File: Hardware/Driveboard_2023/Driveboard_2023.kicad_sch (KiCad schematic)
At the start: 83 parts, among them J1 6P6C, J2 RJ45_LED_Shielded, SW1 SW_Push, SW2 SW_Push, SW3 SW_Push, SW4 SW_Push, SW5 SW_Push, SW6 SW_Push, SW7 SW_SPDT, U1 Teensy4.1_DEV-16771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

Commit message: Assigned Footprints
Assigned footprints
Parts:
- removed D1, D10, D11, D12, D13, D14, D2, D3, D4, D5, D6, D7, D8, D9: 1N4001, Diode_THT:D_DO-41_SOD81_P10.16mm_Horizontal, symbol Diode:1N4001
- added D1, D10, D11, D12, D2, D3, D4, D5, D6, D7, D8, D9: PMEG3015EH, Diode_SMD:D_SOD-123F, symbol Diode:PMEG3015EH
- Conn1: footprint (none) -> MRDT_Connectors:Anderson_2_Horizontal_Side_by_Side_PV
- Conn2, Conn3, Conn4, Conn5, Conn6, Conn7: footprint (none) -> MRDT_Connectors:MOLEX_SL_03_Horizontal
- R17, R19, R21, R23, R25, R27: value 100 -> 10
- SW7: footprint (none) -> Button_Switch_THT:SW_Slide_1P2T_CK_OS102011MS2Q
- U1: footprint MRDT_Shields:MODULE_DEV-16771 -> MRDT_Shields:Teensy_4_1_Vertical
- U2: footprint (none) -> MRDT_Devices:OKI_Horizontal
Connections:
- net BLRX: no longer U1.21 (A7)
- net BLTX: no longer U1.20 (A6)
- net BRRX: now also U1.21 (A7)
- net BRTX: now also U1.20 (A6)
- net MLRX: no longer U1.16 (A2)
- net MLTX: no longer U1.17 (A3)
- net MRRX: now also U1.16 (A2)
- net MRTX: now also U1.17 (A3)
- net at LED15.2 (A): now also D6.1 (K)
- net at R21.2: now also D6.2 (A)
- net at LED19.2 (A): now also D10.1 (K)
- net at R25.2: now also D10.2 (A)
- net at LED21.2 (A): now also D12.1 (K)
- net at R27.2: now also D12.2 (A)
- net at R24.2: now also D9.2 (A)
- net at LED13.2 (A): now also D4.1 (K)
- net at R19.2: now also D4.2 (A)
- net at LED18.2 (A): now also D9.1 (K)
- net at LED14.2 (A): now also D5.1 (K)
- net at R20.2: now also D5.2 (A)
- net at LED20.2 (A): now also D11.1 (K)
- net at R26.2: now also D11.2 (A)
- net at R22.2: now also D7.2 (A)
- net at LED12.2 (A): now also D3.1 (K)
- net at R18.2: now also D3.2 (A)
- net at R16.2: now also D1.2 (A)
- net at LED17.2 (A): now also D8.1 (K)
- net at R23.2: now also D8.2 (A)
- net at R17.2: now also D2.2 (A)
- net at LED11.2 (A): now also D2.1 (K)
- net at R14.2: now also LED8.2 (A)
- net at LED16.2 (A): now also D7.1 (K)
- net at LED9.2 (A): now also R15.2
- net at LED10.2 (A): now also D1.1 (K)

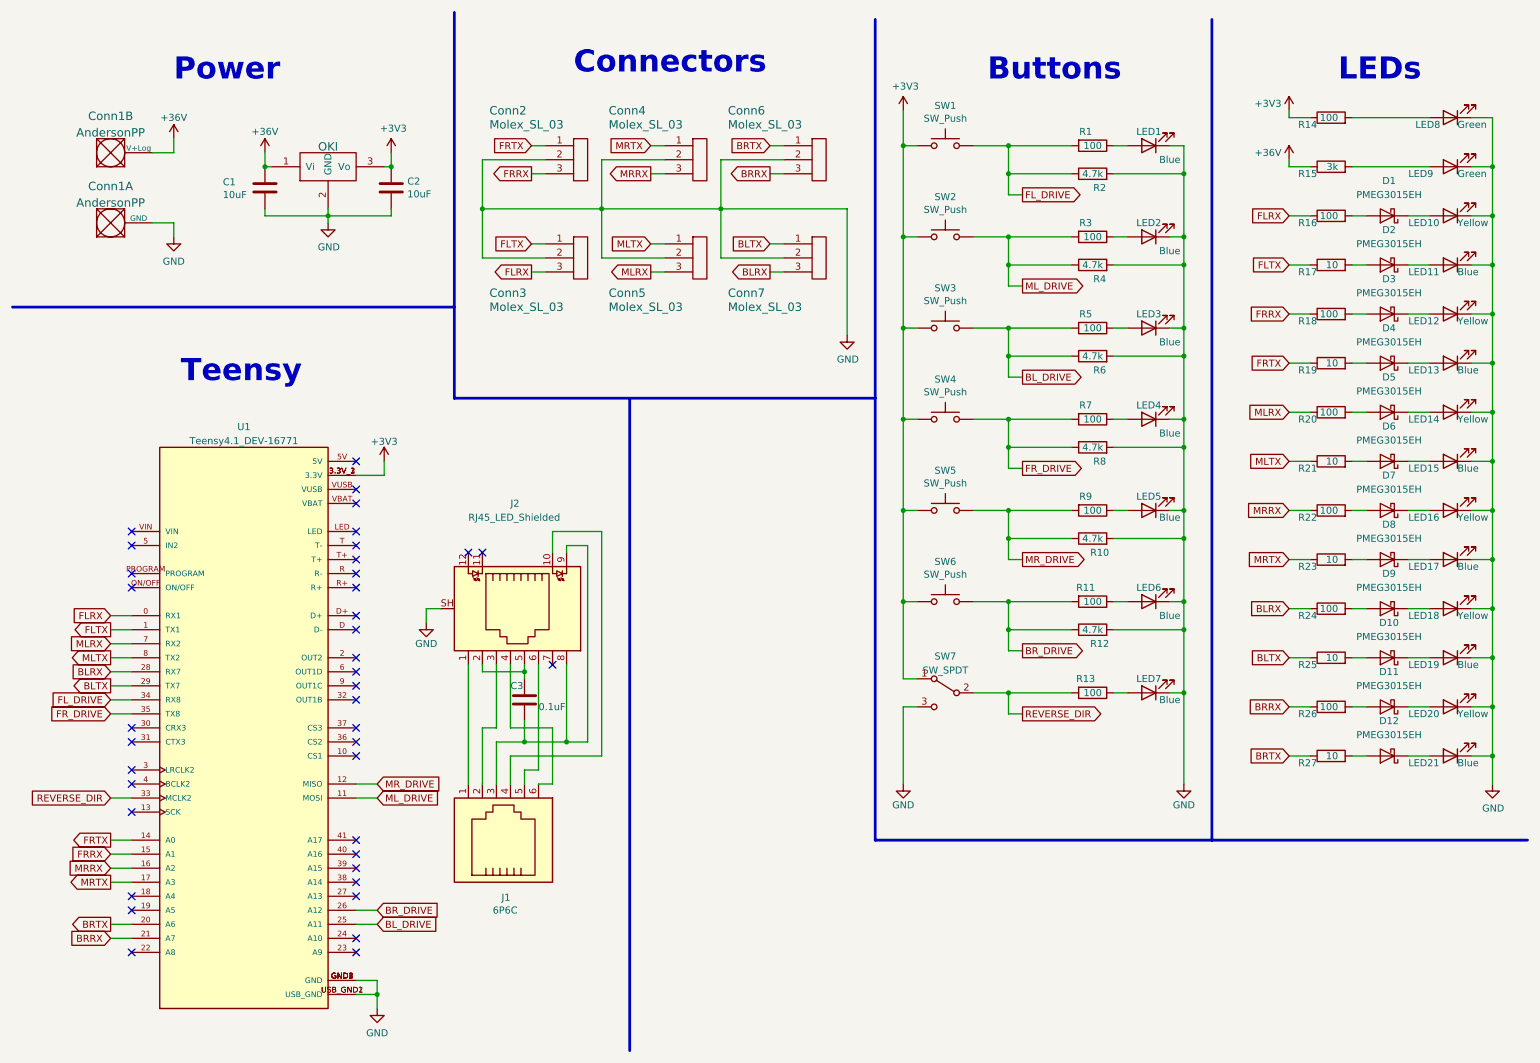
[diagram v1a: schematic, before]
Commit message: PCB Layout
Started and Finished Rev1 of DriveBoard
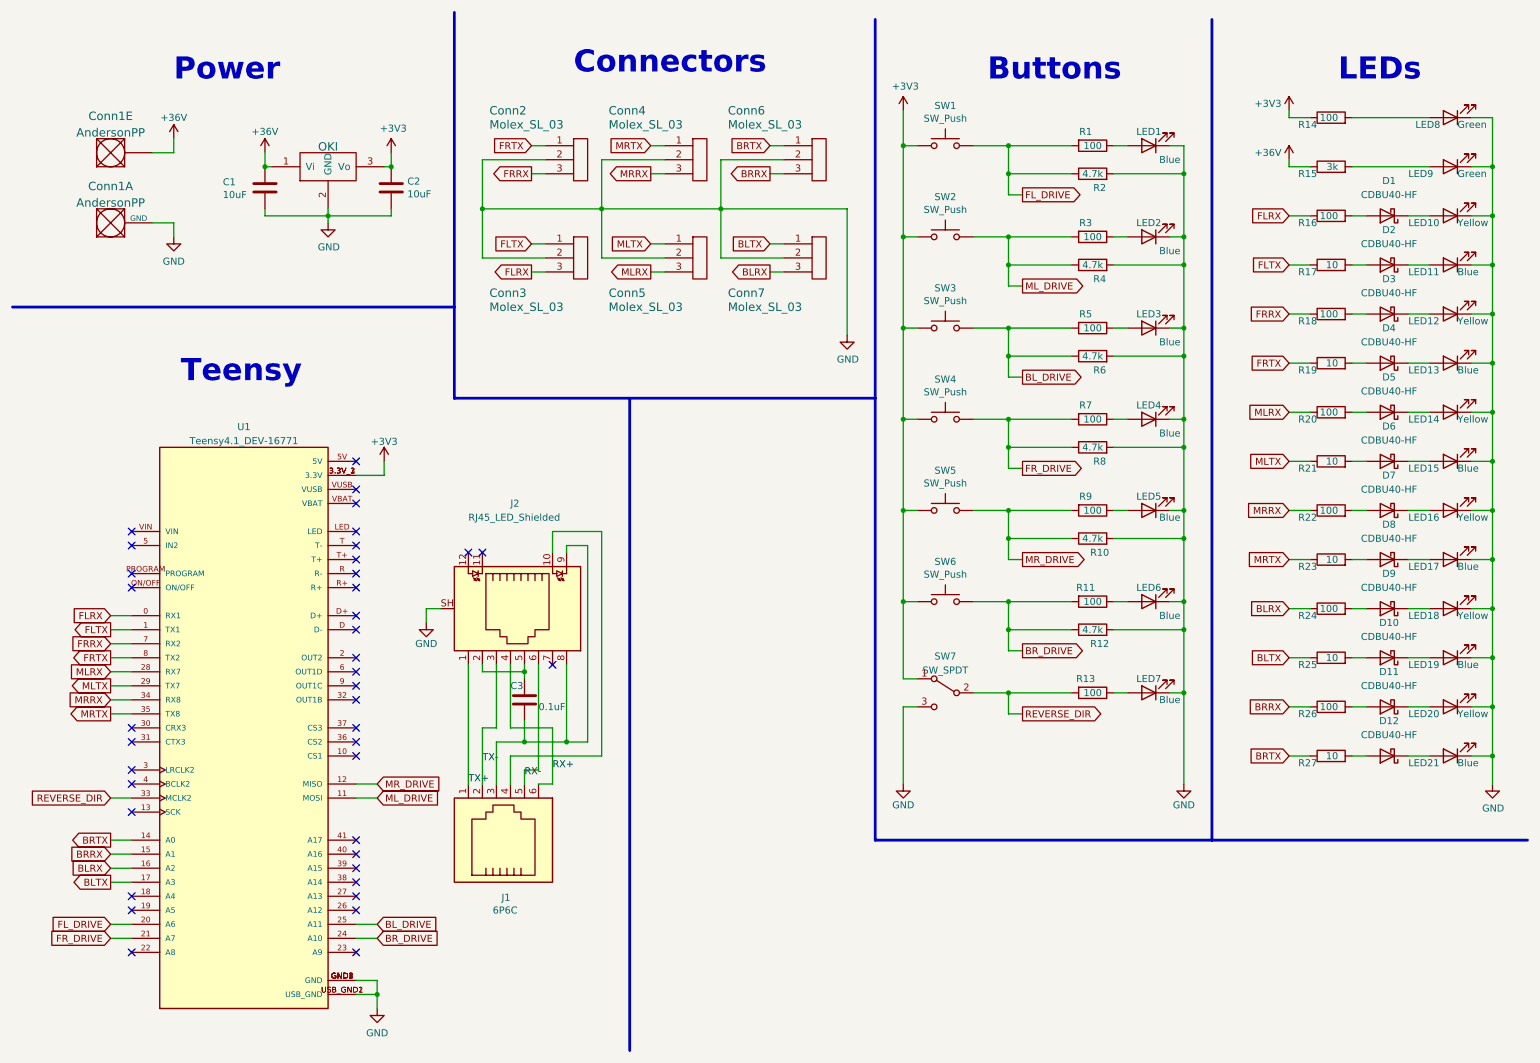
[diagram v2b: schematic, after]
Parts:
- removed D1, D10, D11, D12, D2, D3, D4, D5, D6, D7, D8, D9: PMEG3015EH, Diode_SMD:D_SOD-123F, symbol Diode:PMEG3015EH
- added D1, D10, D11, D12, D2, D3, D4, D5, D6, D7, D8, D9: CDBU40-HF, Diode_SMD:D_0603_1608Metric, symbol Diode:CDBU40-HF
- Conn1: footprint MRDT_Connectors:Anderson_2_Horizontal_Side_by_Side_PV -> MRDT_Connectors:Square_Anderson_2_H_Side_By_Side
- U1: footprint MRDT_Shields:Teensy_4_1_Vertical -> MRDT_Shields:Teensy_4_1
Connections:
- net +36V: now also Conn1.1; no longer Conn1.2 (V+Log)
- net BLRX: now also U1.16 (A2); no longer U1.28 (RX7)
- net BLTX: now also U1.17 (A3); no longer U1.29 (TX7)
- net BRRX: now also U1.15 (A1); no longer U1.21 (A7)
- net BRTX: now also U1.14 (A0); no longer U1.20 (A6)
- net BR_DRIVE: now also U1.24 (A10); no longer U1.26 (A12)
- net FL_DRIVE: now also U1.20 (A6); no longer U1.34 (RX8)
- net FRRX: now also U1.7 (RX2); no longer U1.15 (A1)
- net FRTX: now also U1.8 (TX2); no longer U1.14 (A0)
- net FR_DRIVE: now also U1.21 (A7); no longer U1.35 (TX8)
- net MLRX: now also U1.28 (RX7); no longer U1.7 (RX2)
- net MLTX: now also U1.29 (TX7); no longer U1.8 (TX2)
- net MRRX: now also U1.34 (RX8); no longer U1.16 (A2)
- net MRTX: now also U1.35 (TX8); no longer U1.17 (A3)
- net at R24.2: now also D9.2 (A)
- net at LED20.2 (A): now also D11.1 (K)
- net at R26.2: now also D11.2 (A)
- net at LED21.2 (A): now also D12.1 (K)
- net at LED16.2 (A): now also D7.1 (K)
- net at R22.2: now also D7.2 (A)
- net at LED13.2 (A): now also D4.1 (K)
- net at R19.2: now also D4.2 (A)
- net at LED12.2 (A): now also D3.1 (K)
- net at R18.2: now also D3.2 (A)
- net at LED17.2 (A): now also D8.1 (K)
- net at R23.2: now also D8.2 (A)
- net at LED19.2 (A): now also D10.1 (K)
- net at R25.2: now also D10.2 (A)
- net at LED14.2 (A): now also D5.1 (K)
- net at R20.2: now also D5.2 (A)
- net at LED18.2 (A): now also D9.1 (K)
- net TX+: now reaches J1.1, J2.1
- net TX-: now reaches J1.2, J2.3
- net RX+: now reaches J1.6, J2.4
- net RX-: now reaches J1.5, J2.6
- net at R21.2: now also D6.2 (A)
- net at LED15.2 (A): now also D6.1 (K)
- net at R27.2: now also D12.2 (A)
- net at R16.2: now also D1.2 (A)
- net at R17.2: now also D2.2 (A)
- net at LED11.2 (A): now also D2.1 (K)
- net at LED10.2 (A): now also D1.1 (K)

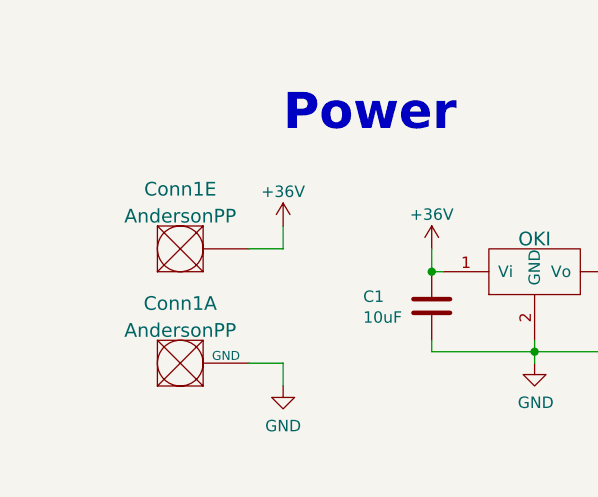
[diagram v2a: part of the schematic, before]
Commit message: Layout Review Board
Finished Changes. Needs to add signatures.
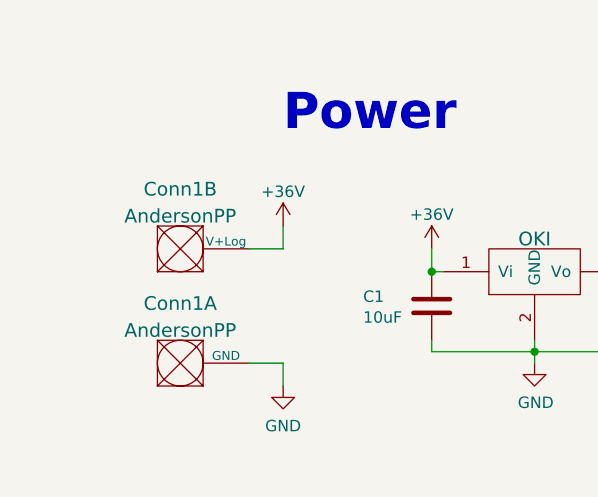
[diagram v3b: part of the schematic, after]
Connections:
- net +36V: now also Conn1.2 (V+Log); no longer Conn1.1
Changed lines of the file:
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@@
     (pin "2")
   )
-  (symbol (lib_id "MRDT_Connectors:AndersonPP") (at 25.4 38.1 0) (unit 5)
+  (symbol (lib_id "MRDT_Connectors:AndersonPP") (at 25.4 38.1 0) (unit 2)
     (in_bom yes) (on_board yes) (fields_autoplaced)
     (property "Reference" "Conn1" (id 0) (at 27.94 28.9359 0)
@@
     )
     (path "/b01ac07b-2202-49d2-b5da-686cdae6ec6c"
-      (reference "Conn1") (unit 5) (value "AndersonPP") (footprint "MRDT_Connectors:Square_Anderson_2_H_Side_By_Side")
+      (reference "Conn1") (unit 2) (value "AndersonPP") (footprint "MRDT_Connectors:Square_Anderson_2_H_Side_By_Side")
     )
     (path "/2efca18a-387a-49fe-a849-7362a7250e39"

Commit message: Layout Review Changes
Fixed the diode's footprints
Labeled many components on PCB
Changed some traces
Added Signature
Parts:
- D1, D10, D11, D12, D2, D3, D4, D5, D6, D7, D8, D9: footprint Diode_SMD:D_0603_1608Metric -> Diode_SMD:D_0603_1608Metric_Pad1.05x0.95mm_HandSolder
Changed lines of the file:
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@@
     (property "Reference" "D9" (id 0) (at 259.3975 111.76 0))
     (property "Value" "CDBU40-HF" (id 1) (at 259.3975 114.3 0))
-    (property "Footprint" "Diode_SMD:D_0603_1608Metric" (id 2) (at 259.08 113.665 0)
+    (property "Footprint" "Diode_SMD:D_0603_1608Metric_Pad1.05x0.95mm_HandSolder" (id 2) (at 259.08 113.665 0)
       (effects (font (size 1.27 1.27)) hide)
     )
@@
     (property "Reference" "D8" (id 0) (at 259.3975 102.87 0))
     (property "Value" "CDBU40-HF" (id 1) (at 259.3975 105.41 0))
-    (property "Footprint" "Diode_SMD:D_0603_1608Metric" (id 2) (at 259.08 104.775 0)
+    (property "Footprint" "Diode_SMD:D_0603_1608Metric_Pad1.05x0.95mm_HandSolder" (id 2) (at 259.08 104.775 0)
       (effects (font (size 1.27 1.27)) hide)
     )
@@
     (property "Reference" "D3" (id 0) (at 259.3975 58.42 0))
     (property "Value" "CDBU40-HF" (id 1) (at 259.3975 60.96 0))
-    (property "Footprint" "Diode_SMD:D_0603_1608Metric" (id 2) (at 259.08 60.325 0)
+    (property "Footprint" "Diode_SMD:D_0603_1608Metric_Pad1.05x0.95mm_HandSolder" (id 2) (at 259.08 60.325 0)
       (effects (font (size 1.27 1.27)) hide)
     )
@@
     (property "Reference" "D10" (id 0) (at 259.3975 120.65 0))
     (property "Value" "CDBU40-HF" (id 1) (at 259.3975 123.19 0))
-    (property "Footprint" "Diode_SMD:D_0603_1608Metric" (id 2) (at 259.08 122.555 0)
+    (property "Footprint" "Diode_SMD:D_0603_1608Metric_Pad1.05x0.95mm_HandSolder" (id 2) (at 259.08 122.555 0)
       (effects (font (size 1.27 1.27)) hide)
     )
@@
     (property "Reference" "D11" (id 0) (at 259.3975 129.54 0))
     (property "Value" "CDBU40-HF" (id 1) (at 259.3975 132.08 0))
-    (property "Footprint" "Diode_SMD:D_0603_1608Metric" (id 2) (at 259.08 131.445 0)
+    (property "Footprint" "Diode_SMD:D_0603_1608Metric_Pad1.05x0.95mm_HandSolder" (id 2) (at 259.08 131.445 0)
       (effects (font (size 1.27 1.27)) hide)
     )
@@
     (property "Reference" "D4" (id 0) (at 259.3975 67.31 0))
     (property "Value" "CDBU40-HF" (id 1) (at 259.3975 69.85 0))
-    (property "Footprint" "Diode_SMD:D_0603_1608Metric" (id 2) (at 259.08 69.215 0)
+    (property "Footprint" "Diode_SMD:D_0603_1608Metric_Pad1.05x0.95mm_HandSolder" (id 2) (at 259.08 69.215 0)
       (effects (font (size 1.27 1.27)) hide)
     )
@@
     (property "Reference" "D6" (id 0) (at 259.3975 85.09 0))
     (property "Value" "CDBU40-HF" (id 1) (at 259.3975 87.63 0))
-    (property "Footprint" "Diode_SMD:D_0603_1608Metric" (id 2) (at 259.08 86.995 0)
+    (property "Footprint" "Diode_SMD:D_0603_1608Metric_Pad1.05x0.95mm_HandSolder" (id 2) (at 259.08 86.995 0)
       (effects (font (size 1.27 1.27)) hide)
     )
@@
     (property "Reference" "D12" (id 0) (at 259.3975 138.43 0))
     (property "Value" "CDBU40-HF" (id 1) (at 259.3975 140.97 0))
-    (property "Footprint" "Diode_SMD:D_0603_1608Metric" (id 2) (at 259.08 140.335 0)
+    (property "Footprint" "Diode_SMD:D_0603_1608Metric_Pad1.05x0.95mm_HandSolder" (id 2) (at 259.08 140.335 0)
       (effects (font (size 1.27 1.27)) hide)
     )
@@
     (property "Reference" "D5" (id 0) (at 259.3975 76.2 0))
     (property "Value" "CDBU40-HF" (id 1) (at 259.3975 78.74 0))
-    (property "Footprint" "Diode_SMD:D_0603_1608Metric" (id 2) (at 259.08 78.105 0)
+    (property "Footprint" "Diode_SMD:D_0603_1608Metric_Pad1.05x0.95mm_HandSolder" (id 2) (at 259.08 78.105 0)
       (effects (font (size 1.27 1.27)) hide)
     )
@@
     (property "Reference" "D7" (id 0) (at 259.3975 93.98 0))
     (property "Value" "CDBU40-HF" (id 1) (at 259.3975 96.52 0))
-    (property "Footprint" "Diode_SMD:D_0603_1608Metric" (id 2) (at 259.08 95.885 0)
+    (property "Footprint" "Diode_SMD:D_0603_1608Metric_Pad1.05x0.95mm_HandSolder" (id 2) (at 259.08 95.885 0)
       (effects (font (size 1.27 1.27)) hide)
     )
@@
     (property "Reference" "D1" (id 0) (at 259.3975 40.64 0))
     (property "Value" "CDBU40-HF" (id 1) (at 259.3975 43.18 0))
-    (property "Footprint" "Diode_SMD:D_0603_1608Metric" (id 2) (at 259.08 42.545 0)
+    (property "Footprint" "Diode_SMD:D_0603_1608Metric_Pad1.05x0.95mm_HandSolder" (id 2) (at 259.08 42.545 0)
       (effects (font (size 1.27 1.27)) hide)
     )
@@
     (property "Reference" "D2" (id 0) (at 259.3975 49.53 0))
     (property "Value" "CDBU40-HF" (id 1) (at 259.3975 52.07 0))
-    (property "Footprint" "Diode_SMD:D_0603_1608Metric" (id 2) (at 259.08 51.435 0)
+    (property "Footprint" "Diode_SMD:D_0603_1608Metric_Pad1.05x0.95mm_HandSolder" (id 2) (at 259.08 51.435 0)
       (effects (font (size 1.27 1.27)) hide)
     )
@@
     )
     (path "/d205b2ca-1ebd-4fd6-a155-856278986126"
-      (reference "D1") (unit 1) (value "CDBU40-HF") (footprint "Diode_SMD:D_0603_1608Metric")
+      (reference "D1") (unit 1) (value "CDBU40-HF") (footprint "Diode_SMD:D_0603_1608Metric_Pad1.05x0.95mm_HandSolder")
     )
     (path "/e04c3c86-869f-4573-98fe-a9086d154c68"
-      (reference "D2") (unit 1) (value "CDBU40-HF") (footprint "Diode_SMD:D_0603_1608Metric")
+      (reference "D2") (unit 1) (value "CDBU40-HF") (footprint "Diode_SMD:D_0603_1608Metric_Pad1.05x0.95mm_HandSolder")
     )
     (path "/78756051-c8fc-49ab-9e31-a0c42b1e03d5"
-      (reference "D3") (unit 1) (value "CDBU40-HF") (footprint "Diode_SMD:D_0603_1608Metric")
+      (reference "D3") (unit 1) (value "CDBU40-HF") (footprint "Diode_SMD:D_0603_1608Metric_Pad1.05x0.95mm_HandSolder")
     )
     (path "/96fe0f79-45ba-44b2-a60f-813456ef0d1e"
-      (reference "D4") (unit 1) (value "CDBU40-HF") (footprint "Diode_SMD:D_0603_1608Metric")
+      (reference "D4") (unit 1) (value "CDBU40-HF") (footprint "Diode_SMD:D_0603_1608Metric_Pad1.05x0.95mm_HandSolder")
     )
     (path "/abf7dae5-9473-4cf8-8a06-d95c49d43f1c"
-      (reference "D5") (unit 1) (value "CDBU40-HF") (footprint "Diode_SMD:D_0603_1608Metric")
+      (reference "D5") (unit 1) (value "CDBU40-HF") (footprint "Diode_SMD:D_0603_1608Metric_Pad1.05x0.95mm_HandSolder")
     )
     (path "/9e75daf8-4fc0-4952-9bca-5efd00661b1e"
-      (reference "D6") (unit 1) (value "CDBU40-HF") (footprint "Diode_SMD:D_0603_1608Metric")
+      (reference "D6") (unit 1) (value "CDBU40-HF") (footprint "Diode_SMD:D_0603_1608Metric_Pad1.05x0.95mm_HandSolder")
     )
     (path "/b4f9a892-f135-435e-abbe-610232474054"
-      (reference "D7") (unit 1) (value "CDBU40-HF") (footprint "Diode_SMD:D_0603_1608Metric")
+      (reference "D7") (unit 1) (value "CDBU40-HF") (footprint "Diode_SMD:D_0603_1608Metric_Pad1.05x0.95mm_HandSolder")
     )
     (path "/5c5bc5f0-cfe0-4dc5-a7be-88cd24d2651b"
-      (reference "D8") (unit 1) (value "CDBU40-HF") (footprint "Diode_SMD:D_0603_1608Metric")
+      (reference "D8") (unit 1) (value "CDBU40-HF") (footprint "Diode_SMD:D_0603_1608Metric_Pad1.05x0.95mm_HandSolder")
     )
     (path "/1837494d-6412-482c-a962-3b20ec4c1118"
-      (reference "D9") (unit 1) (value "CDBU40-HF") (footprint "Diode_SMD:D_0603_1608Metric")
+      (reference "D9") (unit 1) (value "CDBU40-HF") (footprint "Diode_SMD:D_0603_1608Metric_Pad1.05x0.95mm_HandSolder")
     )
     (path "/81e47f23-8c4b-447e-b866-3083bd73182a"
-      (reference "D10") (unit 1) (value "CDBU40-HF") (footprint "Diode_SMD:D_0603_1608Metric")
+      (reference "D10") (unit 1) (value "CDBU40-HF") (footprint "Diode_SMD:D_0603_1608Metric_Pad1.05x0.95mm_HandSolder")
     )
     (path "/8f7faf63-153a-405d-aec7-71b9f1af5769"
-      (reference "D11") (unit 1) (value "CDBU40-HF") (footprint "Diode_SMD:D_0603_1608Metric")
+      (reference "D11") (unit 1) (value "CDBU40-HF") (footprint "Diode_SMD:D_0603_1608Metric_Pad1.05x0.95mm_HandSolder")
     )
     (path "/9f8f86b0-647b-4ef4-8150-f025526550f6"
-      (reference "D12") (unit 1) (value "CDBU40-HF") (footprint "Diode_SMD:D_0603_1608Metric")
+      (reference "D12") (unit 1) (value "CDBU40-HF") (footprint "Diode_SMD:D_0603_1608Metric_Pad1.05x0.95mm_HandSolder")
     )
     (path "/eeeaa791-d0f1-4d41-a4cb-058952f69ac1"
